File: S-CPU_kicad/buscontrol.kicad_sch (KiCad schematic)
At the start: 132 parts, among them U6 IAOO1, U8 IAOO0

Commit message: Schematics tidying in progress.
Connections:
- net wKBNZ renamed wACLK
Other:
- note added: "Inverted SYSCLK"
- note removed: "Inverted CPU CLK"
- company: (none) -> Author: Regis Galland
- title: (none) -> SNES S-CPU Schematics 
- moved on the sheet: HALT, HVCM, LCSG, NBZE, OATK, OBNR, OCEG, OCOG, OCQI, OCSD, OCTG, OCVK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

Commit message: Big update on the hierarchical sheet. DMA section update too.
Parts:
- removed HALT, HVCM, TM: IBUF, symbol Ricoh_Cells:IBUF
- removed LCSG, OCEG, OCQI, OCVK: AND_2, symbol Ricoh_Cells:AND_2
- removed NBZE, OATK, OBNR, OCSD: NAND_2, symbol Ricoh_Cells:NAND_2
- removed OCOG: BUF, symbol Ricoh_Cells:BUF
- removed OCTG: DEMUX_3-8, symbol Ricoh_Cells:DEMUX_3-8
- added GBEG: OR_3, symbol Ricoh_Cells:OR_3
- added MBBX: INVERTER_A, symbol Ricoh_Cells:INVERTER_A
- added MBZG: OR_2, symbol Ricoh_Cells:OR_2
- added ODSN: BUF, symbol Ricoh_Cells:BUF
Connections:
- net DATABUS_LATCH: now also ODSN.2
- net MODE2_OR_MODE3: now also GBEG.3
- net wOCOG_~{MODE7}: now also MBBX.1
- net ~{INTERNAL_CYCLE}: now also GBEG.2
- net wMBLO renamed wMBLO_~{XIN/256}
- new net: MBBX.2, MBZG.2
- new net: MBZG.3, ODSN.1
- new net CPU_RW_EN: GBEG.4
- new net SYNCED_REFRESH_EN: GBEG.1
- new net wSYSCLK: MBZG.1
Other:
- note added: "IARF Goes low during internal CPU cycles VDA and VPA are low and DMA is not running"
- note added: "Latches exernal input data and data bus"
- note removed: "Goes low during internal CPU cycles VDA and VPA are low and DMA is not running"
- note removed: "Modes are active low - inputs seems to be active low MODE7 = Test mode with external CPU connections bypassing 65816 MODE4-6 = DMA test modes MODE0 = SNES mode MODE1 = SNES in halt mode where RDY is used to pause the 65816 MODE2-3 = NES modes where 4200-43FF registers are disabled and CPU connections are external as original idea was probably to include the NES CPU on the board"

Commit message: DMA section update. Found errors between some MUX and MUXI gates.
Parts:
- D7: value IOBUF_A -> IOBUF_B; symbol Ricoh_Cells:IOBUF_A -> Ricoh_Cells:IOBUF_B
- OBWM0, OBWM1: value MUX -> MUXI; symbol Ricoh_Cells:MUX -> Ricoh_Cells:MUXI
- U6: value IAOO1 -> MUX
- U8: value IAOO0 -> MUX
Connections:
- net ~{EXTERNAL_DATA}: now reaches ABVA2.2 (~{ENA}), ABVA2.2 (~{ENA}), ABVA2.2 (~{ENA}), ABVA2.2 (~{ENA}), ABVA2.2 (~{ENA}), ABVA2.2 (~{ENA}), ABVA2.2 (~{ENA}), ABVA2.2 (~{ENA}), ODQC.2
- net at AAXI1.3: now also D7.4 (~{DRV}_HIGH); no longer D7.3 (~{DRV}_HIGH) (x8)
- net ~{INTERNAL_DATA}: now reaches AAXI1.1 (~{ENA}), AAXI1.1 (~{ENA}), AAXI1.1 (~{ENA}), AAXI1.1 (~{ENA}), AAXI1.1 (~{ENA}), AAXI1.1 (~{ENA}), AAXI1.1 (~{ENA}), AAXI1.1 (~{ENA}), ODIB.2
- net RW renamed R~{W}
- net ~{DMA_BUS_ON} renamed HDMA_TABLE_RD
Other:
- note added: "Connected to Data IN Bus enable pins ODQC = '0' to read external data bus"
- note removed: "Connected to Data OUT Bus enable pins ODQC = '0' to read external data bus"

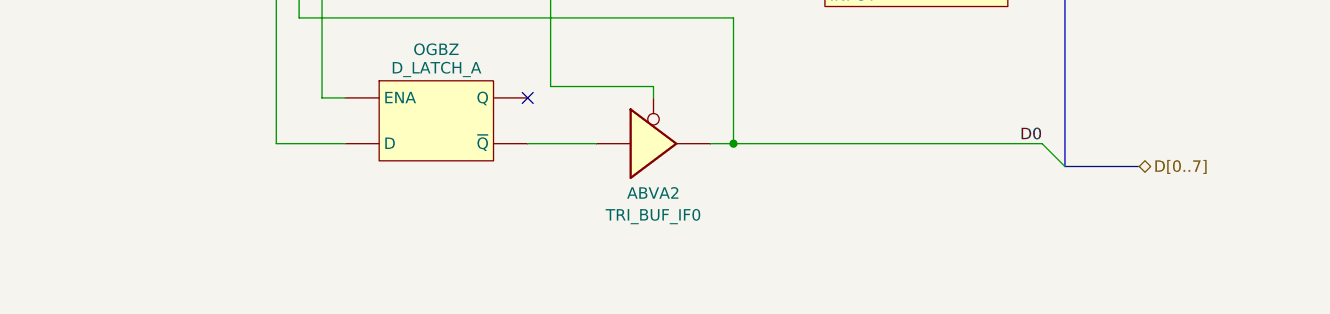
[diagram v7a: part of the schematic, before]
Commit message: HDMA section seems correct after all. More notes added.
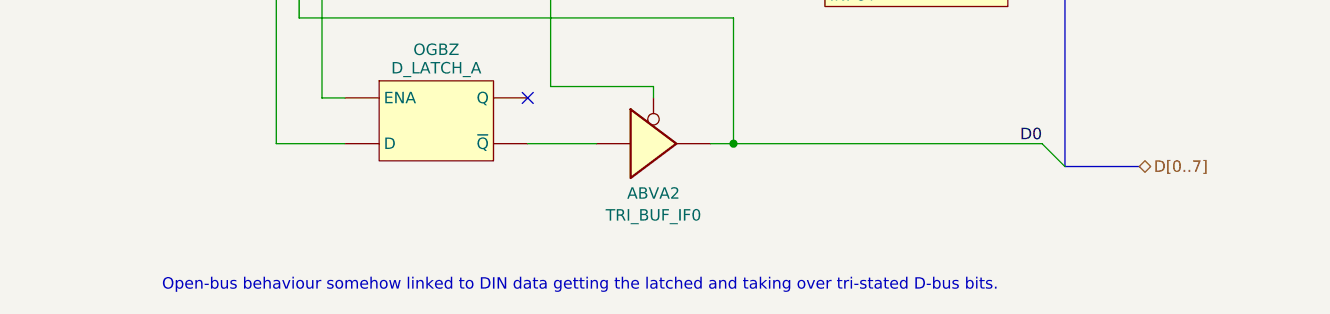
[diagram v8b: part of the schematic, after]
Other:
- note added: "Open-bus behaviour somehow linked to DIN data getting the latched and taking over tri-stated D-bus bits."
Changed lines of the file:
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@@
+    (effects (font (size 1.27 1.27)) (justify left bottom))
+  )
+  (text "Open-bus behaviour somehow linked to DIN data getting the latched and taking over tri-stated D-bus bits."
+    (at 531.495 573.405 0)
     (effects (font (size 1.27 1.27)) (justify left bottom))
   )
